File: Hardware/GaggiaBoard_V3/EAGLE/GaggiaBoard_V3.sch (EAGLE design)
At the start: 68 parts, among them IC1 LD117AS33TR, J1 4PIN, J10 PIN262409-1, J11 PIN262409-1, J12 PIN262409-1, J13 PIN262409-1, J2 Vertical Qwiic Connector, J5 2PIN, J6 3PIN, J7 3PIN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

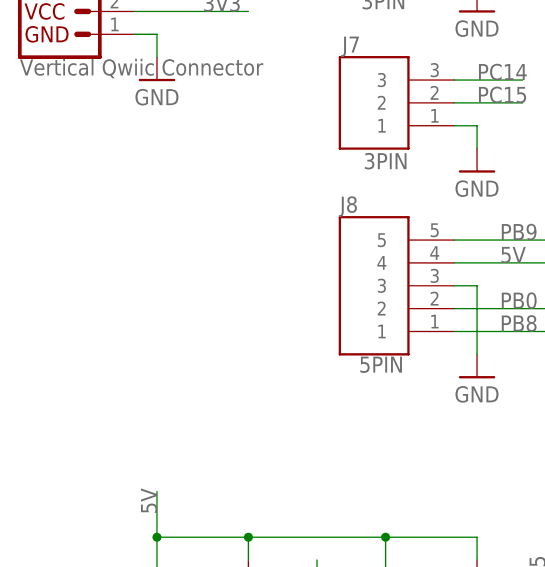
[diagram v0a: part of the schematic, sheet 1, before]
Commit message: UART added
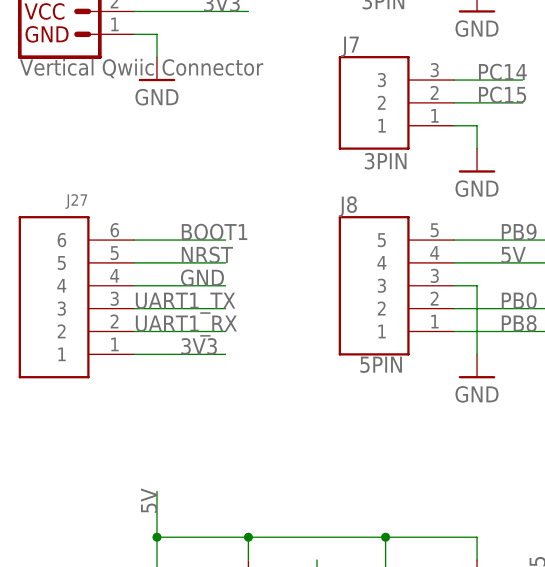
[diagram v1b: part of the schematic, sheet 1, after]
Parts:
- added J27: 6PIN, jst_eph:6PIN
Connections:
- net 3V3: now also J27.1
- net BOOT1: now also J27.6
- net GND: now also J27.4
- net NRST: now also J27.5
- net UART1_RX: now also J27.2
- net UART1_TX: now also J27.3
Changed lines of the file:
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@@
 <part name="MARK7" library="adafruit" library_urn="urn:adsk.eagle:library:420" deviceset="FIDUCIAL" device="" package3d_urn="urn:adsk.eagle:package:6240632/1" override_package3d_urn="urn:adsk.eagle:package:36462288/4" override_package_urn="urn:adsk.eagle:footprint:6239986/1"/>
 <part name="MARK8" library="adafruit" library_urn="urn:adsk.eagle:library:420" deviceset="FIDUCIAL" device="" package3d_urn="urn:adsk.eagle:package:6240632/1" override_package3d_urn="urn:adsk.eagle:package:36462288/4" override_package_urn="urn:adsk.eagle:footprint:6239986/1"/>
+<part name="J27" library="jst_eph" deviceset="6PIN" device="" override_package3d_urn="urn:adsk.eagle:package:37272821/2" override_package_urn="urn:adsk.eagle:footprint:37272822/1">
+<attribute name="LCSC" value="C131342"/>
+</part>
 </parts>
 <sheets>
@@
 <attribute name="NAME" x="12.7" y="180.34" size="1.27" layer="95" rot="R180"/>
 <attribute name="LCSC" x="12.7" y="170.18" size="1.778" layer="96" rot="R180" display="off"/>
+</instance>
+<instance part="J27" gate="G$1" x="12.7" y="119.38" smashed="yes" rot="R180">
+<attribute name="NAME" x="12.7" y="132.08" size="1.27" layer="95" rot="R180"/>
+<attribute name="LCSC" x="12.7" y="119.38" size="1.778" layer="96" rot="R180" display="off"/>
 </instance>
 </instances>
@@
 <wire x1="17.78" y1="167.64" x2="30.48" y2="167.64" width="0.1524" layer="91"/>
 <label x="25.4" y="167.64" size="1.778" layer="95"/>
+</segment>
+<segment>
+<pinref part="J27" gate="G$1" pin="4"/>
+<wire x1="17.78" y1="121.92" x2="27.94" y2="121.92" width="0.1524" layer="91"/>
+<label x="22.86" y="121.92" size="1.778" layer="95"/>
 </segment>
 </net>
@@
 <junction x="132.08" y="167.64"/>
 </segment>
+<segment>
+<pinref part="J27" gate="G$1" pin="1"/>
+<wire x1="17.78" y1="114.3" x2="27.94" y2="114.3" width="0.1524" layer="91"/>
+<label x="22.86" y="114.3" size="1.778" layer="95"/>
+</segment>
 </net>
 <net name="I2C2_SDA" class="0">
@@
 <label x="172.72" y="154.94" size="1.778" layer="95"/>
 </segment>
+<segment>
+<pinref part="J27" gate="G$1" pin="3"/>
+<wire x1="17.78" y1="119.38" x2="27.94" y2="119.38" width="0.1524" layer="91"/>
+<label x="17.78" y="119.38" size="1.778" layer="95"/>
+</segment>
 </net>
 <net name="UART1_RX" class="0">
@@
 <label x="172.72" y="152.4" size="1.778" layer="95"/>
 </segment>
+<segment>
+<pinref part="J27" gate="G$1" pin="2"/>
+<wire x1="17.78" y1="116.84" x2="27.94" y2="116.84" width="0.1524" layer="91"/>
+<label x="17.78" y="116.84" size="1.778" layer="95"/>
+</segment>
 </net>
 <net name="NRST" class="0">
@@
 <wire x1="218.44" y1="129.54" x2="231.14" y2="129.54" width="0.1524" layer="91"/>
 <label x="226.06" y="129.54" size="1.778" layer="95"/>
+</segment>
+<segment>
+<pinref part="J27" gate="G$1" pin="5"/>
+<wire x1="17.78" y1="124.46" x2="27.94" y2="124.46" width="0.1524" layer="91"/>
+<label x="22.86" y="124.46" size="1.778" layer="95"/>
 </segment>
 </net>
@@
 <label x="226.06" y="157.48" size="1.778" layer="95"/>
 </segment>
-</net>
+<segment>
+<pinref part="J27" gate="G$1" pin="6"/>
+<wire x1="17.78" y1="127" x2="27.94" y2="127" width="0.1524" layer="91"/>
+<label x="22.86" y="127" size="1.778" layer="95"/>
+</segment>
+</net>

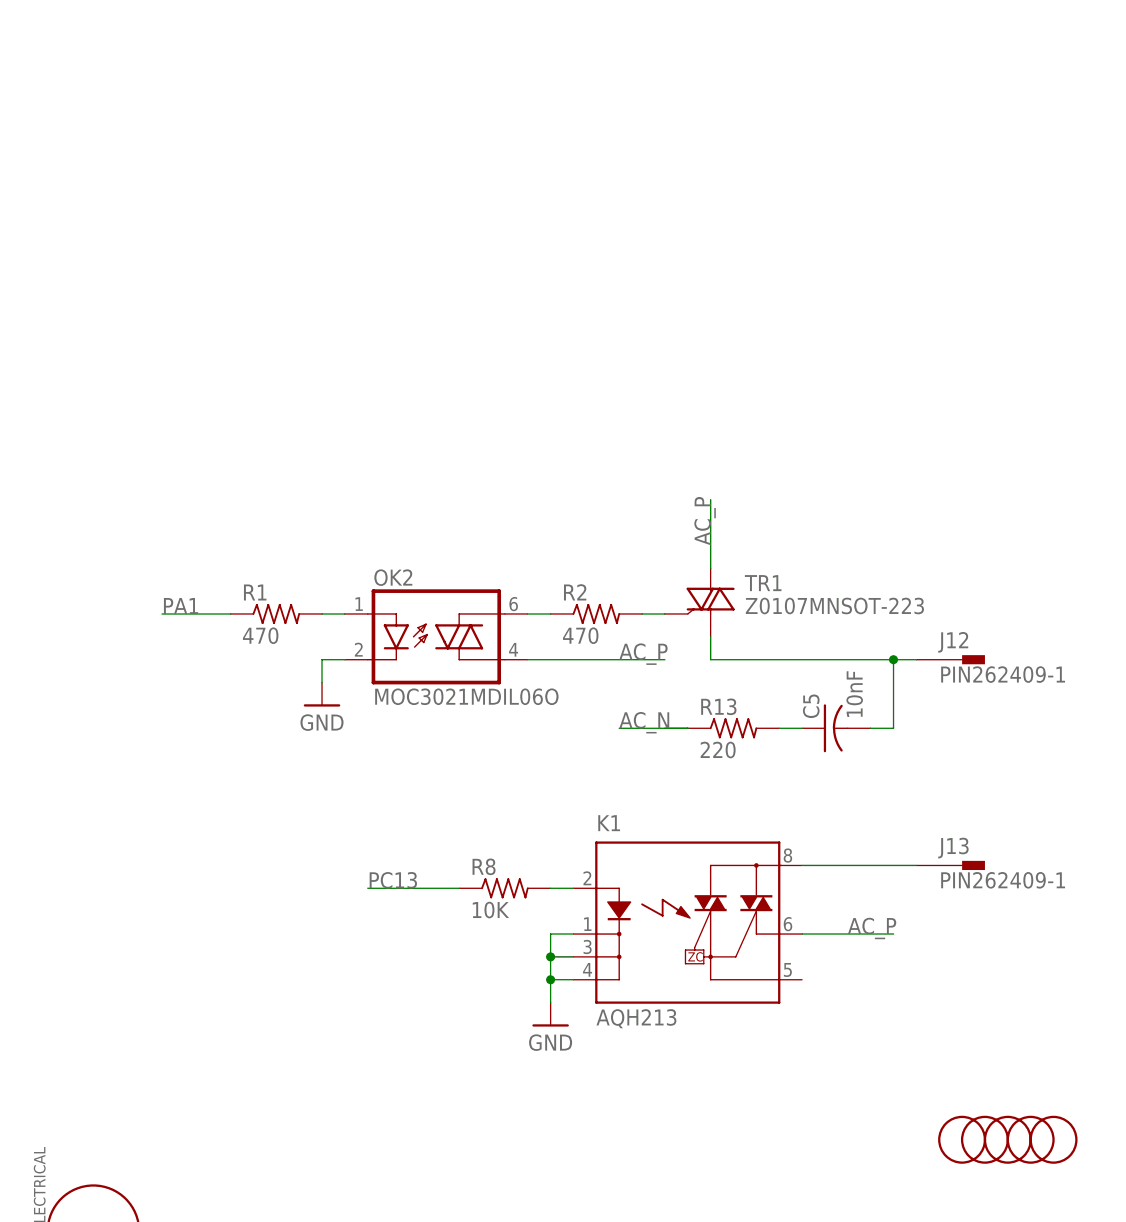
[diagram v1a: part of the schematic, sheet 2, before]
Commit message: README + PC13 load fix
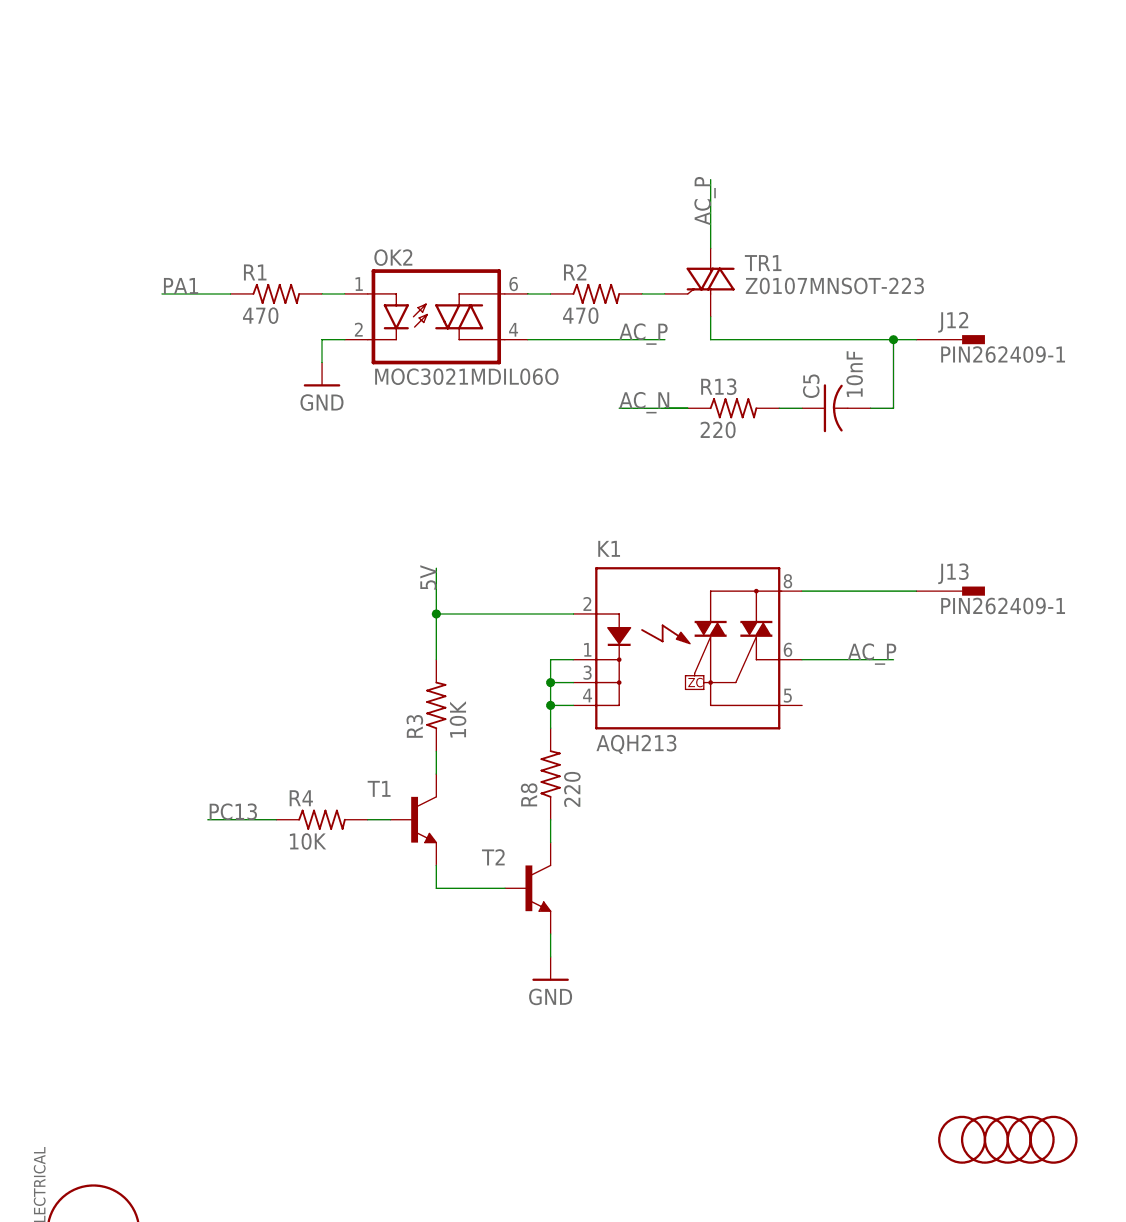
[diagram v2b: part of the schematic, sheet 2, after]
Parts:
- added R3, R4: 10K, rcl:R-US_R0603
- added T1, T2: (no value), transistor:MMBT2222ALT1-NPN-SOT23-BEC
- R8: value 10K -> 220; LCSC C98220 -> C107696
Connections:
- new net N$11: R8.1, T2.C
- new net N$12: T1.E, T2.B
- new net N$13: K1.K, K1.K1, K1.K2, R8.2
- new net N$14: R4.2, T1.B
- net 5V: now also K1.A, R3.2
- net GND: now also T2.E; no longer K1.K, K1.K1, K1.K2
- net N$1: now also R3.1, T1.C; no longer K1.A, R8.2
- net PC13: now also R4.1; no longer R8.1
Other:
- moved on the sheet: C5, J12, J13, K1, OK2, R1, R13, R2, R8, TR1

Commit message: J1 fix
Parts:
- PSU1: LCSC (none) -> C2857903
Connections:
- net 5V: now also J1.1; no longer J1.4
- net GND: now also J1.4; no longer J1.1
- net UART2_RX: now also J1.2; no longer J1.3
- net UART2_TX: now also J1.3; no longer J1.2
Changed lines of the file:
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@@
 <part name="SUPPLY22" library="Power_Symbols" library_urn="urn:adsk.eagle:library:16502351" deviceset="GND-BAR" device="" value="GND"/>
 <part name="PSU1" library="discrete" deviceset="IRM-10-5" device="" override_package3d_urn="urn:adsk.eagle:package:36415007/2" override_package_urn="urn:adsk.eagle:footprint:36415008/1" override_locally_modified="yes">
+<attribute name="LCSC" value="C2857903"/>
 <attribute name="SPICEPREFIX" value="E"/>
 </part>
@@
 </segment>
 <segment>
-<pinref part="J1" gate="G$1" pin="1"/>
-<wire x1="17.78" y1="167.64" x2="30.48" y2="167.64" width="0.1524" layer="91"/>
-<label x="25.4" y="167.64" size="1.778" layer="95"/>
+<label x="20.32" y="175.26" size="1.778" layer="95"/>
+<wire x1="17.78" y1="175.26" x2="30.48" y2="175.26" width="0.1524" layer="91"/>
+<pinref part="J1" gate="G$1" pin="4"/>
 </segment>
 <segment>
@@
 </segment>
 <segment>
-<pinref part="J1" gate="G$1" pin="4"/>
-<wire x1="17.78" y1="175.26" x2="30.48" y2="175.26" width="0.1524" layer="91"/>
-<label x="27.94" y="175.26" size="1.778" layer="95"/>
+<label x="20.32" y="167.64" size="1.778" layer="95"/>
+<wire x1="17.78" y1="167.64" x2="30.48" y2="167.64" width="0.1524" layer="91"/>
+<pinref part="J1" gate="G$1" pin="1"/>
 </segment>
 </net>
@@
 </segment>
 <segment>
-<pinref part="J1" gate="G$1" pin="3"/>
-<wire x1="17.78" y1="172.72" x2="30.48" y2="172.72" width="0.1524" layer="91"/>
-<label x="17.78" y="172.72" size="1.778" layer="95"/>
+<label x="20.32" y="170.18" size="1.778" layer="95"/>
+<wire x1="17.78" y1="170.18" x2="30.48" y2="170.18" width="0.1524" layer="91"/>
+<pinref part="J1" gate="G$1" pin="2"/>
 </segment>
 </net>
@@
 </segment>
 <segment>
-<pinref part="J1" gate="G$1" pin="2"/>
-<wire x1="17.78" y1="170.18" x2="30.48" y2="170.18" width="0.1524" layer="91"/>
-<label x="17.78" y="170.18" size="1.778" layer="95"/>
+<label x="20.32" y="172.72" size="1.778" layer="95"/>
+<wire x1="17.78" y1="172.72" x2="30.48" y2="172.72" width="0.1524" layer="91"/>
+<pinref part="J1" gate="G$1" pin="3"/>
 </segment>
 </net>
@@
 <attribute name="NAME" x="38.1" y="25.4" size="1.27" layer="95"/>
 <attribute name="VALUE" x="38.1" y="10.16" size="1.27" layer="96"/>
+<attribute name="LCSC" x="45.72" y="17.78" size="1.778" layer="96" display="off"/>
 </instance>
 <instance part="SUPPLY23" gate="G$1" x="60.96" y="10.16" smashed="yes">

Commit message: snubbers
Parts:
- added C16: 10nF, rcl:C-USC1206
- added R5: 220, rcl:R-US_R2512
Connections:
- removed net N$32: C5.1, R13.2
- new net N$15: C16.2, R5.1
- new net N$16: C5.2, R13.1
- net 3WAY: now also R5.2
- net AC_N: no longer R13.1
- net AC_P: now also C16.1, C5.1
- net PUMP_P: now also R13.2; no longer C5.2
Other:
- moved on the sheet: C5, R13
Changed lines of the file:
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@@
 <attribute name="LCSC" value="C98220"/>
+</part>
+<part name="R5" library="rcl" library_urn="urn:adsk.eagle:library:334" deviceset="R-US_" device="R2512" package3d_urn="urn:adsk.eagle:package:23545/2" value="220">
+<spice>
+<pinmapping spiceprefix="R">
+<pinmap gate="G$1" pin="1" pinorder="1"/>
+<pinmap gate="G$1" pin="2" pinorder="2"/>
+</pinmapping>
+</spice>
+<attribute name="LCSC" value="C877859"/>
+</part>
+<part name="C16" library="rcl" library_urn="urn:adsk.eagle:library:334" deviceset="C-US" device="C1206" package3d_urn="urn:adsk.eagle:package:23618/2" value="10nF">
+<spice>
+<pinmapping spiceprefix="C">
+<pinmap gate="G$1" pin="1" pinorder="1"/>
+<pinmap gate="G$1" pin="2" pinorder="2"/>
+</pinmapping>
+</spice>
+<attribute name="LCSC" value="C107192"/>
 </part>
 </parts>
@@
 <instance part="MARK4" gate="G$1" x="243.84" y="27.94" smashed="yes"/>
 <instance part="MARK3" gate="G$1" x="241.3" y="27.94" smashed="yes"/>
-<instance part="R13" gate="G$1" x="208.28" y="109.22" smashed="yes">
-<attribute name="NAME" x="204.47" y="110.7186" size="1.778" layer="95"/>
-<attribute name="VALUE" x="204.47" y="105.918" size="1.778" layer="96"/>
-<attribute name="LCSC" x="208.28" y="109.22" size="1.778" layer="96" display="off"/>
-</instance>
-<instance part="C5" gate="G$1" x="218.44" y="109.22" smashed="yes" rot="R90">
-<attribute name="NAME" x="217.805" y="110.236" size="1.778" layer="95" rot="R90"/>
-<attribute name="VALUE" x="222.631" y="110.236" size="1.778" layer="96" rot="R90"/>
-<attribute name="LCSC" x="218.44" y="109.22" size="1.778" layer="96" rot="R90" display="off"/>
+<instance part="R13" gate="G$1" x="218.44" y="109.22" smashed="yes">
+<attribute name="NAME" x="214.63" y="110.7186" size="1.778" layer="95"/>
+<attribute name="VALUE" x="214.63" y="105.918" size="1.778" layer="96"/>
+<attribute name="LCSC" x="218.44" y="109.22" size="1.778" layer="96" display="off"/>
+</instance>
+<instance part="C5" gate="G$1" x="205.74" y="109.22" smashed="yes" rot="R90">
+<attribute name="NAME" x="205.105" y="110.236" size="1.778" layer="95" rot="R90"/>
+<attribute name="VALUE" x="209.931" y="110.236" size="1.778" layer="96" rot="R90"/>
+<attribute name="LCSC" x="205.74" y="109.22" size="1.778" layer="96" rot="R90" display="off"/>
 </instance>
 <instance part="MARK6" gate="G$1" x="238.76" y="27.94" smashed="yes"/>
@@
 <attribute name="LCSC" x="162.56" y="63.5" size="1.778" layer="96" display="off"/>
 </instance>
+<instance part="R5" gate="G$1" x="218.44" y="96.52" smashed="yes">
+<attribute name="NAME" x="214.63" y="98.0186" size="1.778" layer="95"/>
+<attribute name="VALUE" x="214.63" y="93.218" size="1.778" layer="96"/>
+<attribute name="LCSC" x="218.44" y="96.52" size="1.778" layer="96" display="off"/>
+</instance>
+<instance part="C16" gate="G$1" x="205.74" y="96.52" smashed="yes" rot="R90">
+<attribute name="NAME" x="205.105" y="97.536" size="1.778" layer="95" rot="R90"/>
+<attribute name="VALUE" x="209.931" y="97.536" size="1.778" layer="96" rot="R90"/>
+<attribute name="LCSC" x="205.74" y="96.52" size="1.778" layer="96" rot="R90" display="off"/>
+</instance>
 </instances>
 <busses>
@@
 </segment>
 <segment>
-<label x="195.58" y="109.22" size="1.778" layer="95"/>
-<pinref part="R13" gate="G$1" pin="1"/>
-<wire x1="203.2" y1="109.22" x2="200.66" y2="109.22" width="0.1524" layer="91"/>
-<wire x1="195.58" y1="109.22" x2="203.2" y2="109.22" width="0.1524" layer="91"/>
-</segment>
-<segment>
 <label x="5.08" y="68.58" size="1.778" layer="95"/>
 <wire x1="15.24" y1="68.58" x2="5.08" y2="68.58" width="0.1524" layer="91"/>
@@
 <segment>
 <pinref part="OK2" gate="G$1" pin="A1"/>
-<wire x1="185.42" y1="116.84" x2="200.66" y2="116.84" width="0.1524" layer="91"/>
+<wire x1="185.42" y1="116.84" x2="193.04" y2="116.84" width="0.1524" layer="91"/>
 <label x="195.58" y="116.84" size="1.778" layer="95"/>
+<pinref part="C5" gate="G$1" pin="1"/>
+<wire x1="193.04" y1="116.84" x2="200.66" y2="116.84" width="0.1524" layer="91"/>
+<wire x1="203.2" y1="109.22" x2="193.04" y2="109.22" width="0.1524" layer="91"/>
+<wire x1="193.04" y1="109.22" x2="193.04" y2="116.84" width="0.1524" layer="91"/>
+<junction x="193.04" y="116.84"/>
+<pinref part="C16" gate="G$1" pin="1"/>
+<wire x1="203.2" y1="96.52" x2="193.04" y2="96.52" width="0.1524" layer="91"/>
+<wire x1="193.04" y1="96.52" x2="193.04" y2="109.22" width="0.1524" layer="91"/>
+<junction x="193.04" y="109.22"/>
 </segment>
 <segment>
@@
 <net name="3WAY" class="0">
 <segment>
-<wire x1="228.6" y1="88.9" x2="215.9" y2="88.9" width="0.1524" layer="91"/>
+<wire x1="228.6" y1="88.9" x2="226.06" y2="88.9" width="0.1524" layer="91"/>
 <pinref part="J13" gate="-1" pin="1"/>
 <pinref part="K1" gate="G$1" pin="DS1"/>
+<pinref part="R5" gate="G$1" pin="2"/>
+<wire x1="226.06" y1="88.9" x2="215.9" y2="88.9" width="0.1524" layer="91"/>
+<wire x1="223.52" y1="96.52" x2="226.06" y2="96.52" width="0.1524" layer="91"/>
+<wire x1="226.06" y1="96.52" x2="226.06" y2="88.9" width="0.1524" layer="91"/>
+<junction x="226.06" y="88.9"/>
 </segment>
 </net>
@@
 </segment>
 </net>
-<net name="N$32" class="0">
-<segment>
-<pinref part="C5" gate="G$1" pin="1"/>
-<pinref part="R13" gate="G$1" pin="2"/>
-<wire x1="215.9" y1="109.22" x2="213.36" y2="109.22" width="0.1524" layer="91"/>
-</segment>
-</net>
 <net name="PUMP_P" class="0">
 <segment>
 <pinref part="J12" gate="-1" pin="1"/>
 <wire x1="228.6" y1="116.84" x2="226.06" y2="116.84" width="0.1524" layer="91"/>
+<pinref part="TR1" gate="G$1" pin="A1"/>
 <wire x1="226.06" y1="116.84" x2="205.74" y2="116.84" width="0.1524" layer="91"/>
-<pinref part="C5" gate="G$1" pin="2"/>
+<wire x1="205.74" y1="116.84" x2="205.74" y2="119.38" width="0.1524" layer="91"/>
+<pinref part="R13" gate="G$1" pin="2"/>
 <wire x1="223.52" y1="109.22" x2="226.06" y2="109.22" width="0.1524" layer="91"/>
 <wire x1="226.06" y1="109.22" x2="226.06" y2="116.84" width="0.1524" layer="91"/>
 <junction x="226.06" y="116.84"/>
-<pinref part="TR1" gate="G$1" pin="A1"/>
-<wire x1="205.74" y1="116.84" x2="205.74" y2="119.38" width="0.1524" layer="91"/>
 </segment>
 </net>
@@
 </segment>
 </net>
+<net name="N$15" class="0">
+<segment>
+<pinref part="R5" gate="G$1" pin="1"/>
+<pinref part="C16" gate="G$1" pin="2"/>
+<wire x1="213.36" y1="96.52" x2="210.82" y2="96.52" width="0.1524" layer="91"/>
+</segment>
+</net>
+<net name="N$16" class="0">
+<segment>
+<pinref part="R13" gate="G$1" pin="1"/>
+<pinref part="C5" gate="G$1" pin="2"/>
+<wire x1="213.36" y1="109.22" x2="210.82" y2="109.22" width="0.1524" layer="91"/>
+</segment>
+</net>

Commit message: J4 p/n fix
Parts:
- J4: LCSC C474893 -> C474892
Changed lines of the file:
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@@
 </part>
 <part name="J4" library="SparkFun-Connectors" deviceset="CONN_02" device="3.5MM-NO_SILK" override_package3d_urn="urn:adsk.eagle:package:36462297/4" override_package_urn="urn:adsk.eagle:footprint:36462298/2">
-<attribute name="LCSC" value="C474893"/>
+<attribute name="LCSC" value="C474892"/>
 </part>
 <part name="C15" library="rcl" library_urn="urn:adsk.eagle:library:334" deviceset="C-US" device="C0603" package3d_urn="urn:adsk.eagle:package:23616/2" value="0.1uF">
